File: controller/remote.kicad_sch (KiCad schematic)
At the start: 12 parts, among them J1 Conn_01x03, J7 MC130VX

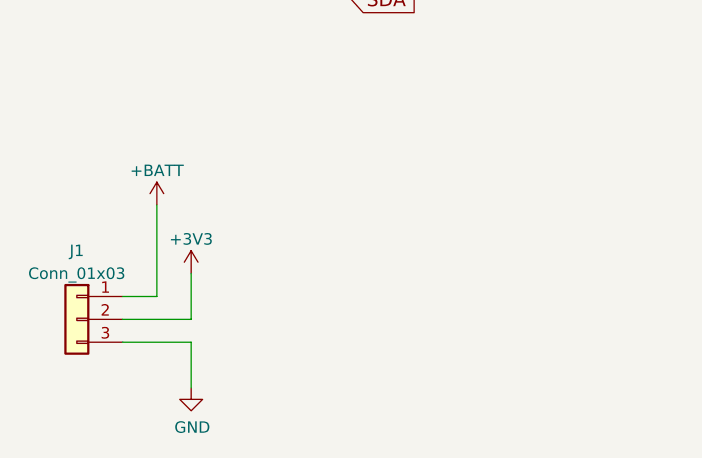
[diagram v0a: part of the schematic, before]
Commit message: Add test point.
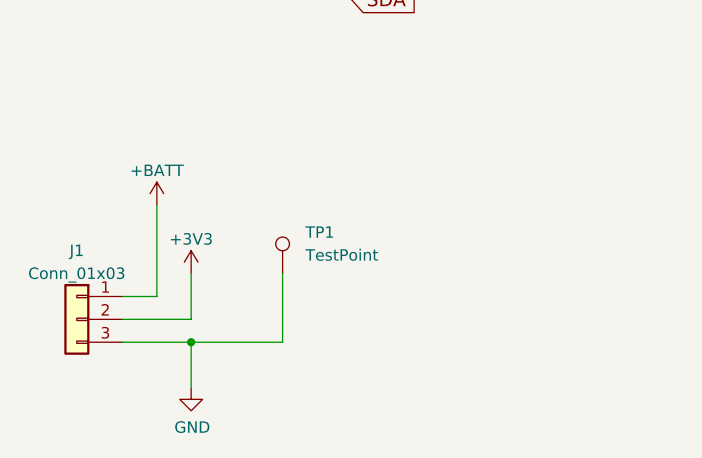
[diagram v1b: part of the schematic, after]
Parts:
- added TP1: TestPoint, TestPoint:TestPoint_Keystone_5000-5004_Miniature, symbol Connector:TestPoint
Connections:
- net GND: now also TP1.1
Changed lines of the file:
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@@
+	)
+	(junction
+		(at 45.72 101.6)
+		(diameter 0)
+		(color 0 0 0 0)
 	)
 	(junction
@@
 	(wire
 		(pts
+			(xy 55.88 101.6) (xy 45.72 101.6)
+		)
+		(stroke
+			(width 0)
+			(type default)
+		)
+	)
+	(wire
+		(pts
 			(xy 39.37 43.18) (xy 41.91 43.18)
 		)
@@
 		(pts
 			(xy 38.1 99.06) (xy 45.72 99.06)
+		)
+		(stroke
+			(width 0)
+			(type default)
+		)
+	)
+	(wire
+		(pts
+			(xy 55.88 93.98) (xy 55.88 101.6)
 		)
 		(stroke
@@
 					(unit 1)
 				)
+			)
+		)
+	)
+	(symbol
+		(lib_id "Connector:TestPoint")
+		(at 55.88 93.98 0)
+		(unit 1)
+		(exclude_from_sim no)
+		(in_bom yes)
+		(on_board yes)
+		(dnp no)
+		(fields_autoplaced yes)
+		(property "Reference" "TP1"
+			(at 58.42 89.4079 0)
+			(effects
+				(font
+					(size 1.27 1.27)
+				)
+				(justify left)
+			)
+		)
+		(property "Value" "TestPoint"
+			(at 58.42 91.9479 0)
+			(effects
+				(font
+					(size 1.27 1.27)
+				)
+				(justify left)
+			)
+		)
+		(property "Footprint" "TestPoint:TestPoint_Keystone_5000-5004_Miniature"
+			(at 60.96 93.98 0)
+			(effects
+				(font
+					(size 1.27 1.27)
+				)
+				(hide yes)
+			)
+		)
+		(property "Datasheet" "~"
+			(at 60.96 93.98 0)
+			(effects
+				(font
+					(size 1.27 1.27)
+				)
+				(hide yes)
+			)
+		)
+		(property "Description" "test point"
+			(at 55.88 93.98 0)
+			(effects
+				(font
+					(size 1.27 1.27)
+				)
+				(hide yes)
+			)
+		)
+		(pin "1"
+		)
+		(instances
+			(project ""
+				(path "/0776e334-fbf5-4a46-a47e-c7e0521e2a6b"
+					(reference "TP1")
+					(unit 1)
+				)

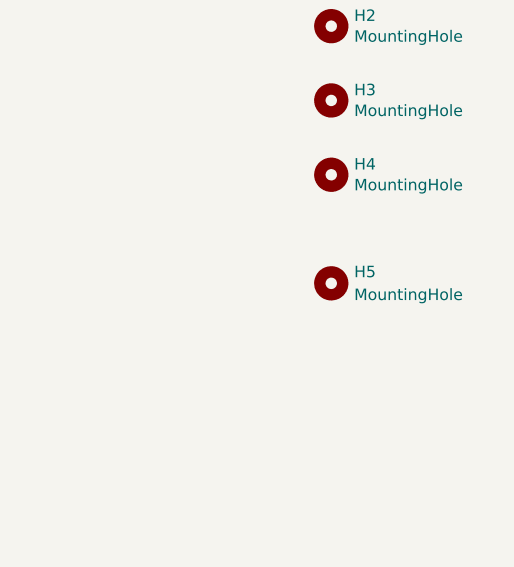
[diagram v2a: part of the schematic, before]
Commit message: Remove nRF24L01.
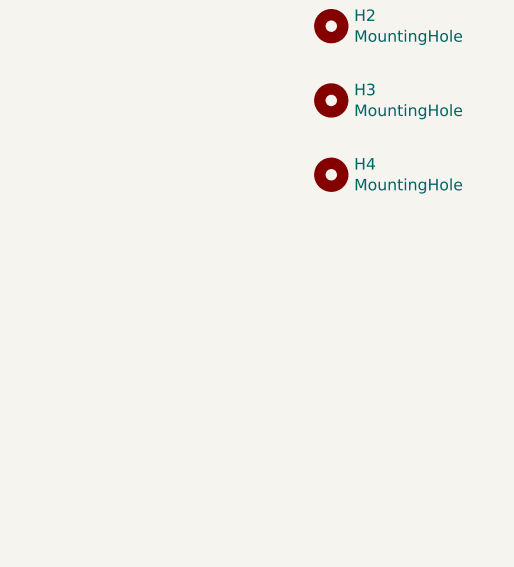
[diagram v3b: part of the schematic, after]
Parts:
- removed H5: MountingHole, MountingHole:MountingHole_2.2mm_M2, symbol Mechanical:MountingHole
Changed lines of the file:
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@@
 (kicad_sch
-	(version 20240812)
+	(version 20241004)
 	(generator "eeschema")
 	(generator_version "8.99")
@@
 					(unit 1)
 				)
-			)
-		)
-	)
-	(symbol
-		(lib_id "Mechanical:MountingHole")
-		(at 261.62 55.88 0)
-		(unit 1)
-		(exclude_from_sim no)
-		(in_bom yes)
-		(on_board yes)
-		(dnp no)
-		(fields_autoplaced yes)
-		(property "Reference" "H5"
-			(at 264.16 54.6099 0)
-			(effects
-				(font
-					(size 1.27 1.27)
-				)
-				(justify left)
-			)
-		)
-		(property "Value" "MountingHole"
-			(at 264.16 57.1499 0)
-			(effects
-				(font
-					(size 1.27 1.27)
-				)
-				(justify left)
-			)
-		)
-		(property "Footprint" "MountingHole:MountingHole_2.2mm_M2"
-			(at 261.62 55.88 0)
-			(effects
-				(font
-					(size 1.27 1.27)
-				)
-				(hide yes)
-			)
-		)
-		(property "Datasheet" "~"
-			(at 261.62 55.88 0)
-			(effects
-				(font
-					(size 1.27 1.27)
-				)
-				(hide yes)
-			)
-		)
-		(property "Description" "Mounting Hole without connection"
-			(at 261.62 55.88 0)
-			(effects
-				(font
-					(size 1.27 1.27)
-				)
-				(hide yes)
-			)
-		)
-		(instances
-			(project "remote"
-				(path "/0776e334-fbf5-4a46-a47e-c7e0521e2a6b"
-					(reference "H5")
-					(unit 1)
-				)

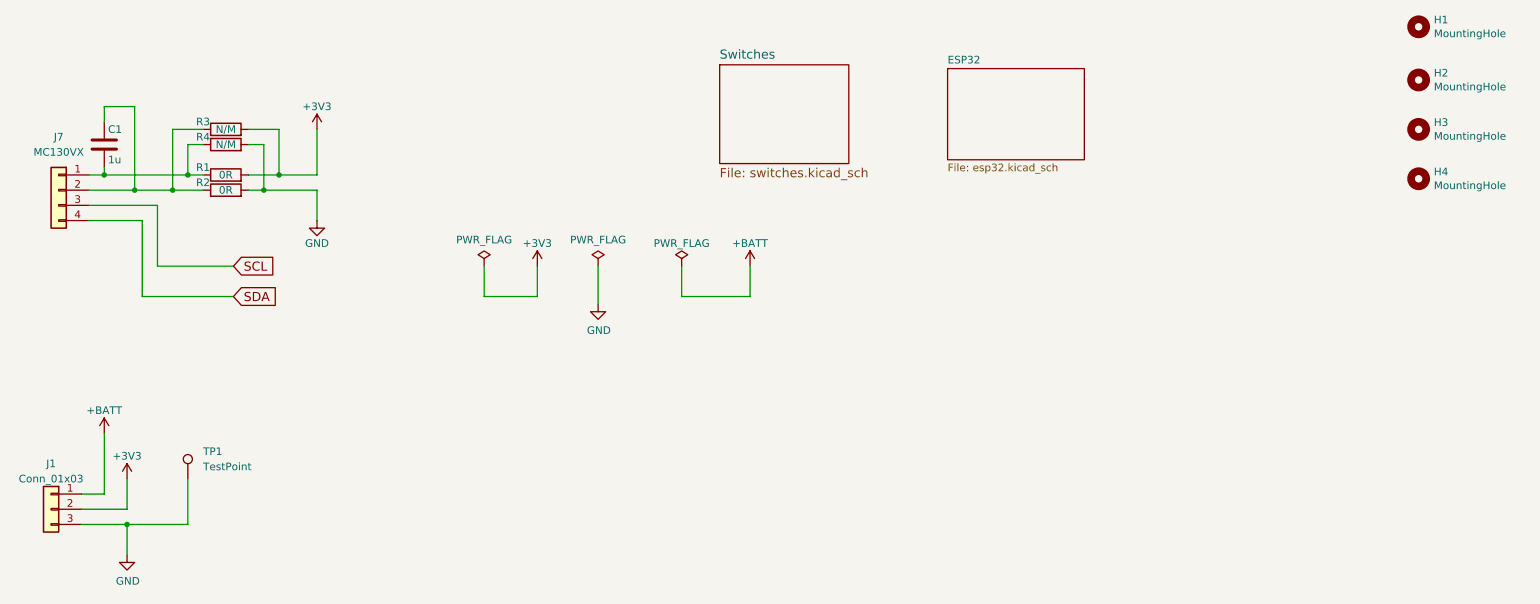
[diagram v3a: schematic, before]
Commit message: Power directly from battery.
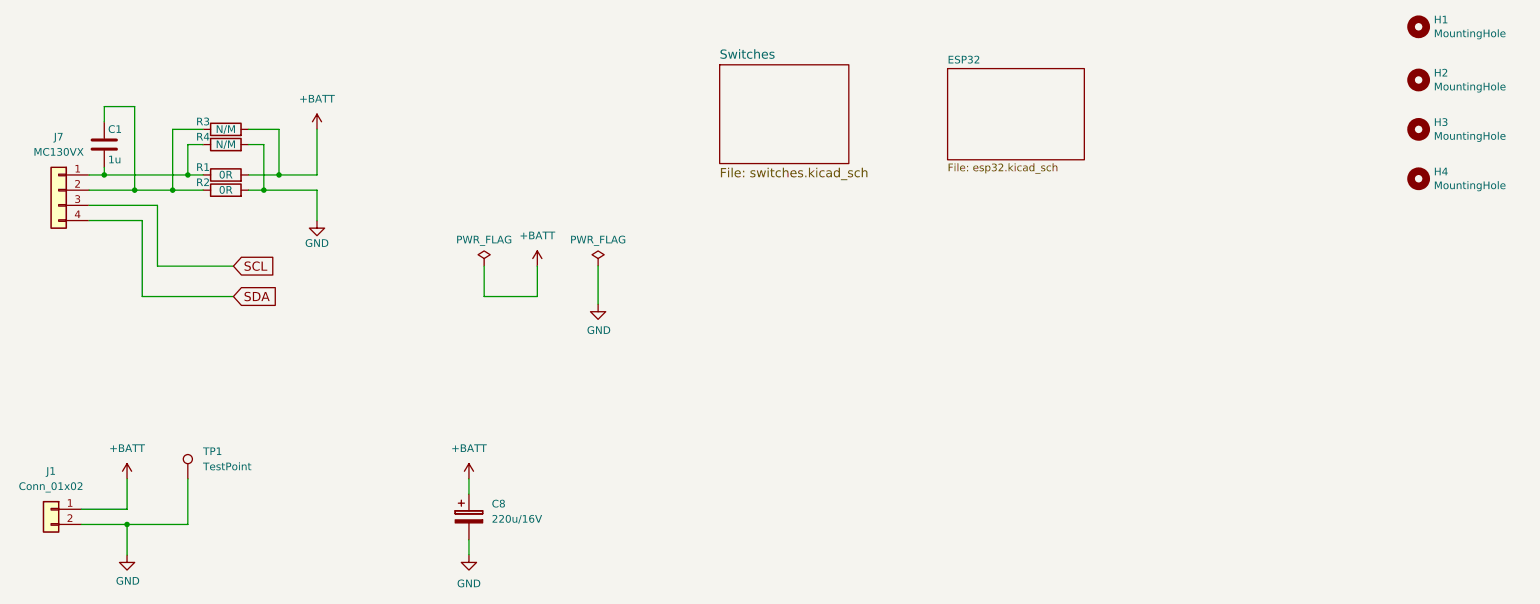
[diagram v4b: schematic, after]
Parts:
- removed J1: Conn_01x03, Connector_JST:JST_XH_B03B-XH-A_1x03_P2.50mm_Vertical, symbol Connector_Generic:Conn_01x03
- added C8: 220u/16V, symbol Device:CP
- added J1: Conn_01x02, Connector_JST:JST_XH_B02B-XH-A_1x02_P2.50mm_Vertical, symbol Connector_Generic:Conn_01x02
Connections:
- net +3V3 is gone; now on net +BATT: R1.2, R3.2
- net +BATT: now also C8.1, J1.1 (Pin_1)
- net GND: now also C8.2, J1.2 (Pin_2)

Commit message: Add large decoupling cap.
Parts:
- C8: footprint (none) -> Capacitor_SMD:CP_Elec_10x10.5
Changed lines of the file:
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@@
 			)
 		)
-		(property "Footprint" ""
+		(property "Footprint" "Capacitor_SMD:CP_Elec_10x10.5"
 			(at 103.8352 104.14 0)
 			(effects

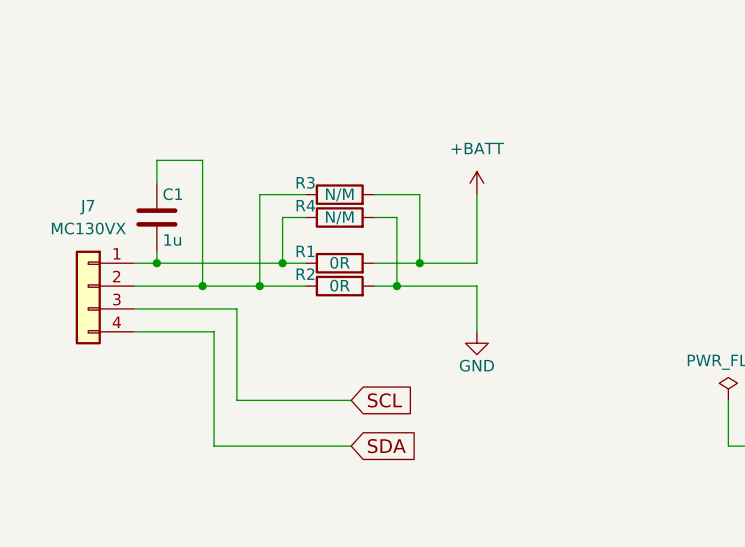
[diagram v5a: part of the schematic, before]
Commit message: Make mounting R1/R2 optional.
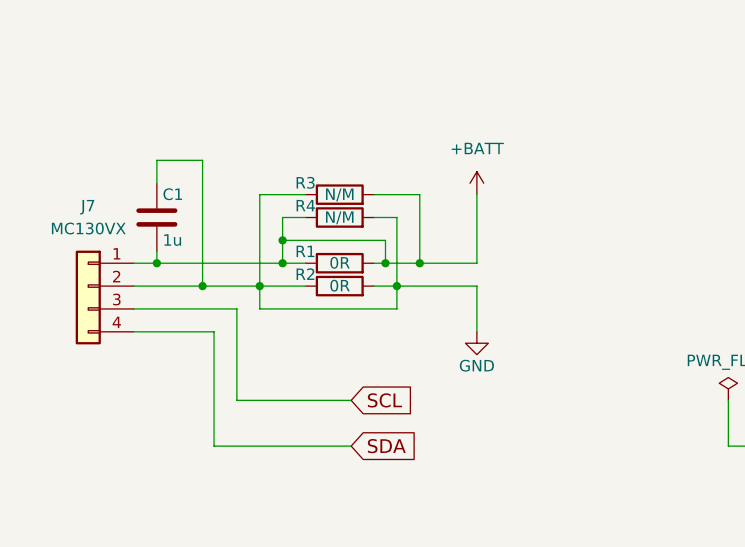
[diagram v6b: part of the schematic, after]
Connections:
- net +BATT: now also C1.2, J7.1 (Pin_1), R1.1, R4.1
- net GND: now also C1.1, J7.2 (Pin_2), R2.1, R3.1
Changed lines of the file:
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@@
+	)
+	(junction
+		(at 55.88 40.64)
+		(diameter 0)
+		(color 0 0 0 0)
 	)
 	(junction
@@
 	)
 	(junction
+		(at 67.31 43.18)
+		(diameter 0)
+		(color 0 0 0 0)
+	)
+	(junction
 		(at 71.12 43.18)
 		(diameter 0)
@@
 	(wire
 		(pts
+			(xy 67.31 43.18) (xy 67.31 40.64)
+		)
+		(stroke
+			(width 0)
+			(type default)
+		)
+	)
+	(wire
+		(pts
 			(xy 45.72 99.06) (xy 45.72 93.98)
 		)
@@
 	(wire
 		(pts
-			(xy 55.88 38.1) (xy 55.88 43.18)
+			(xy 55.88 38.1) (xy 55.88 40.64)
+		)
+		(stroke
+			(width 0)
+			(type default)
+		)
+	)
+	(wire
+		(pts
+			(xy 68.58 48.26) (xy 68.58 45.72)
 		)
 		(stroke
@@
 	(wire
 		(pts
+			(xy 53.34 45.72) (xy 53.34 48.26)
+		)
+		(stroke
+			(width 0)
+			(type default)
+		)
+	)
+	(wire
+		(pts
 			(xy 39.37 45.72) (xy 46.99 45.72)
 		)
@@
 	(wire
 		(pts
+			(xy 53.34 48.26) (xy 68.58 48.26)
+		)
+		(stroke
+			(width 0)
+			(type default)
+		)
+	)
+	(wire
+		(pts
 			(xy 46.99 45.72) (xy 53.34 45.72)
 		)
@@
 	(wire
 		(pts
+			(xy 67.31 40.64) (xy 55.88 40.64)
+		)
+		(stroke
+			(width 0)
+			(type default)
+		)
+	)
+	(wire
+		(pts
 			(xy 41.91 34.29) (xy 41.91 31.75)
 		)
@@
 	(wire
 		(pts
-			(xy 66.04 43.18) (xy 71.12 43.18)
+			(xy 66.04 43.18) (xy 67.31 43.18)
 		)
 		(stroke
@@
 		)
 		(stroke
+			(width 0)
+			(type default)
+		)
+	)
+	(wire
+		(pts
+			(xy 55.88 40.64) (xy 55.88 43.18)
+		)
+		(stroke
+			(width 0)
+			(type default)
+		)
+	)
+	(wire
+		(pts
+			(xy 67.31 43.18) (xy 71.12 43.18)
+		)
+		(stroke
